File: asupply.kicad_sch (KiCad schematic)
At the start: 94 parts, among them U10 LT3081xDF, U11 LT3042xMSE, U12 LT3045xMSE, U13 LT3045xMSE, U14 LT3042xMSE, U15 LT3094xMSE, U16 LT3042xMSE, U9 LTC3261

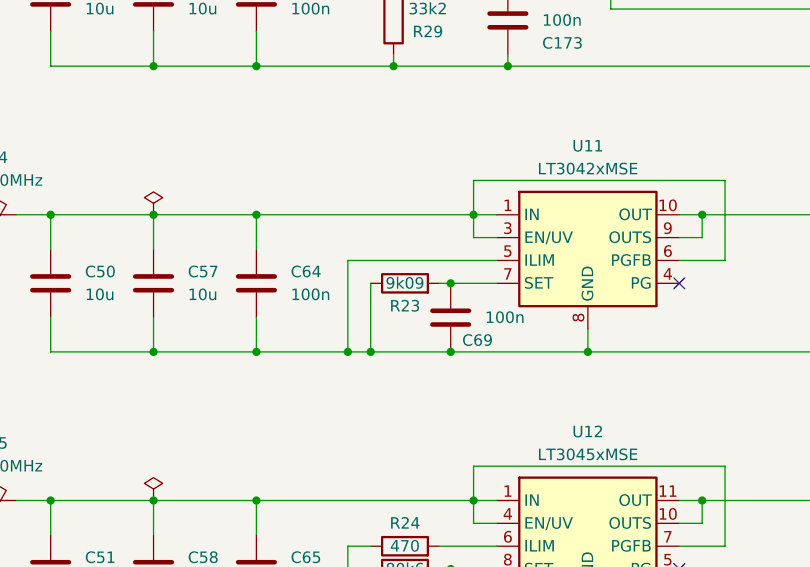
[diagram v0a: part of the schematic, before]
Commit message: add V01 production files, bug fixes
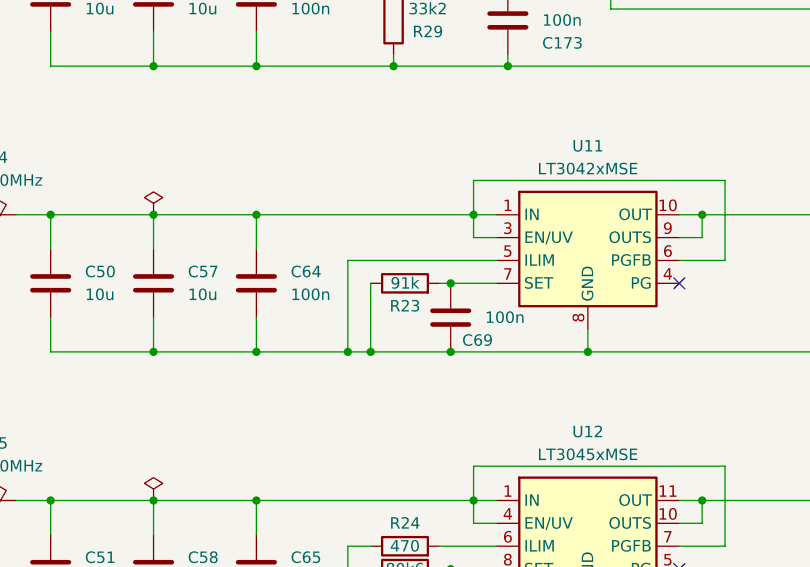
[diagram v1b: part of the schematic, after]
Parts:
- R23: value 9k09 -> 91k
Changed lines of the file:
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@@
     (in_bom yes) (on_board yes)
     (property "Reference" "R23" (id 0) (at 203.2 86.36 90))
-    (property "Value" "9k09" (id 1) (at 203.2 83.82 90))
+    (property "Value" "91k" (id 1) (at 203.2 83.82 90))
     (property "Footprint" "Resistor_SMD:R_0603_1608Metric" (id 2) (at 203.2 85.598 90)
       (effects (font (size 1.27 1.27) bold) hide)

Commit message: v 0.2 schematics
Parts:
- removed C173: 100n, Capacitor_SMD:C_0603_1608Metric, symbol Device:C
- added R?: 51k, Resistor_SMD:R_0603_1608Metric, symbol Device:R
- added TP11, TP12, TP13, TP14, TP15, TP16, TP17, TP18, TP19: TestPoint, TestPoint:TestPoint_Pad_2.0x2.0mm, symbol Connector:TestPoint
- R23: value 91k -> 9k09
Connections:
- net +15V: now also TP19.1
- net +3.3VA: now also TP17.1
- net +5VA: now also TP16.1
- net +8V: now also TP15.1
- net +9V: now also TP13.1
- net +9VA: now also TP14.1
- net -6V: now also TP18.1
- net -9V: now also TP12.1
- net GND: now also R?.1
- net +1V8: now reaches C35.1, C39.1, D5.1 (K), FB8.1
- net +1V8: now also TP11.1
- net LD_EN: now reaches U12.5 (PG)
- net LD_EN: now also R?.2
- no-connect marks 8 -> 7
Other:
- moved on the sheet: C75, C82, C89, U10

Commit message: fixes
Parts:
- added C?: 100n, Capacitor_SMD:C_0603_1608Metric, symbol Device:C
- added C?: 220u, Capacitor_Tantalum_SMD:CP_EIA-7343-15_Kemet-W, symbol Device:C_Polarized
- added C?: 10u, Capacitor_SMD:C_0805_2012Metric, symbol Device:C
- added L?: 1u, Inductor_SMD:L_1008_2520Metric, symbol Device:L
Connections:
- net +9V: now also L?.1; no longer FB2.2
- net GND: now also C?.2, C?.2, C?.2
- new net: C?.1, C?.1, C?.1, FB2.2, L?.2
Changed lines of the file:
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@@
   (junction (at 254 237.49) (diameter 0) (color 0 0 0 0)
   )
+  (junction (at 111.76 168.91) (diameter 0) (color 0 0 0 0)
+  )
   (junction (at 163.83 76.2) (diameter 0) (color 0 0 0 0)
   )
@@
   (junction (at 175.26 107.95) (diameter 0) (color 0 0 0 0)
   )
+  (junction (at 85.09 168.91) (diameter 0) (color 0 0 0 0)
+  )
   (junction (at 196.85 91.44) (diameter 0) (color 0 0 0 0)
   )
@@
   (junction (at 254 219.71) (diameter 0) (color 0 0 0 0)
   )
+  (junction (at 97.79 168.91) (diameter 0) (color 0 0 0 0)
+  )
   (junction (at 148.59 201.93) (diameter 0) (color 0 0 0 0)
   )
@@
   (junction (at 254 201.93) (diameter 0) (color 0 0 0 0)
   )
+  (junction (at 85.09 176.53) (diameter 0) (color 0 0 0 0)
+  )
   (junction (at 110.49 201.93) (diameter 0) (color 0 0 0 0)
   )
@@
   (junction (at 281.94 59.69) (diameter 0) (color 0 0 0 0)
   )
+  (junction (at 97.79 176.53) (diameter 0) (color 0 0 0 0)
+  )
   (junction (at 267.97 59.69) (diameter 0) (color 0 0 0 0)
   )
@@
     (stroke (width 0) (type default) (color 0 0 0 0))
   )
+  (wire (pts (xy 85.09 176.53) (xy 97.79 176.53))
+    (stroke (width 0) (type default) (color 0 0 0 0))
+  )
   (wire (pts (xy 207.01 115.57) (xy 208.28 115.57))
     (stroke (width 0) (type default) (color 0 0 0 0))
@@
     (stroke (width 0) (type default) (color 0 0 0 0))
   )
+  (wire (pts (xy 85.09 168.91) (xy 97.79 168.91))
+    (stroke (width 0) (type default) (color 0 0 0 0))
+  )
   (wire (pts (xy 163.83 59.69) (xy 175.26 59.69))
     (stroke (width 0) (type default) (color 0 0 0 0))
@@
     (stroke (width 0) (type default) (color 0 0 0 0))
   )
+  (wire (pts (xy 115.57 168.91) (xy 111.76 168.91))
+    (stroke (width 0) (type default) (color 0 0 0 0))
+  )
+  (wire (pts (xy 123.19 168.91) (xy 125.73 168.91))
+    (stroke (width 0) (type default) (color 0 0 0 0))
+  )
   (wire (pts (xy 267.97 44.45) (xy 281.94 44.45))
     (stroke (width 0) (type default) (color 0 0 0 0))
@@
     (stroke (width 0) (type default) (color 0 0 0 0))
   )
-  (wire (pts (xy 73.66 189.23) (xy 73.66 193.04))
+  (wire (pts (xy 73.66 168.91) (xy 73.66 193.04))
     (stroke (width 0) (type default) (color 0 0 0 0))
   )
@@
     (stroke (width 0) (type default) (color 0 0 0 0))
   )
+  (wire (pts (xy 73.66 168.91) (xy 85.09 168.91))
+    (stroke (width 0) (type default) (color 0 0 0 0))
+  )
   (wire (pts (xy 267.97 237.49) (xy 267.97 241.3))
     (stroke (width 0) (type default) (color 0 0 0 0))
@@
     (stroke (width 0) (type default) (color 0 0 0 0))
   )
+  (wire (pts (xy 111.76 168.91) (xy 97.79 168.91))
+    (stroke (width 0) (type default) (color 0 0 0 0))
+  )
   (wire (pts (xy 186.69 111.76) (xy 186.69 107.95))
     (stroke (width 0) (type default) (color 0 0 0 0))
@@
     (stroke (width 0) (type default) (color 0 0 0 0))
   )
+  (wire (pts (xy 111.76 176.53) (xy 97.79 176.53))
+    (stroke (width 0) (type default) (color 0 0 0 0))
+  )
   (wire (pts (xy 186.69 184.15) (xy 196.85 184.15))
     (stroke (width 0) (type default) (color 0 0 0 0))
@@
     (pin "2")
   )
+  (symbol (lib_id "Device:C") (at 85.09 172.72 0) (mirror y) (unit 1)
+    (in_bom yes) (on_board yes) (fields_autoplaced)
+    (property "Reference" "C?" (id 0) (at 81.28 171.4499 0)
+      (effects (font (size 1.27 1.27)) (justify left))
+    )
+    (property "Value" "100n" (id 1) (at 81.28 173.9899 0)
+      (effects (font (size 1.27 1.27)) (justify left))
+    )
+    (property "Footprint" "Capacitor_SMD:C_0603_1608Metric" (id 2) (at 84.1248 176.53 0)
+      (effects (font (size 1.27 1.27)) hide)
+    )
+    (property "Datasheet" "~" (id 3) (at 85.09 172.72 0)
+      (effects (font (size 1.27 1.27)) hide)
+    )
+    (property "MFR_PN" "CL10B104KB8NNWC" (id 4) (at 85.09 172.72 0)
+      (effects (font (size 1.27 1.27)) hide)
+    )
+    (property "MFR_PN_ALT" "CL10B104KB8NNNL" (id 5) (at 85.09 172.72 0)
+      (effects (font (size 1.27 1.27)) hide)
+    )
+    (pin "1")
+    (pin "2")
+  )
   (symbol (lib_id "Device:C") (at 254 83.82 0) (unit 1)
     (in_bom yes) (on_board yes) (fields_autoplaced)
@@
     (pin "2")
   )
+  (symbol (lib_id "Device:C_Polarized") (at 111.76 172.72 0) (mirror y) (unit 1)
+    (in_bom yes) (on_board yes) (fields_autoplaced)
+    (property "Reference" "C?" (id 0) (at 107.95 170.5609 0)
+      (effects (font (size 1.27 1.27)) (justify left))
+    )
+    (property "Value" "220u" (id 1) (at 107.95 173.1009 0)
+      (effects (font (size 1.27 1.27)) (justify left))
+    )
+    (property "Footprint" "Capacitor_Tantalum_SMD:CP_EIA-7343-15_Kemet-W" (id 2) (at 110.7948 176.53 0)
+      (effects (font (size 1.27 1.27)) hide)
+    )
+    (property "Datasheet" "~" (id 3) (at 111.76 172.72 0)
+      (effects (font (size 1.27 1.27)) hide)
+    )
+    (property "MFR_PN" "T491D227K016AT" (id 4) (at 111.76 172.72 0)
+      (effects (font (size 1.27 1.27)) hide)
+    )
+    (property "MFR_PN_ALT" "293D227X9016E2TE3" (id 5) (at 111.76 172.72 0)
+      (effects (font (size 1.27 1.27)) hide)
+    )
+    (pin "1")
+    (pin "2")
+  )
   (symbol (lib_id "Device:C") (at 254 245.11 0) (unit 1)
     (in_bom yes) (on_board yes) (fields_autoplaced)
@@
     (pin "2")
   )
+  (symbol (lib_id "Device:C") (at 97.79 172.72 0) (mirror y) (unit 1)
+    (in_bom yes) (on_board yes) (fields_autoplaced)
+    (property "Reference" "C?" (id 0) (at 93.98 171.4499 0)
+      (effects (font (size 1.27 1.27)) (justify left))
+    )
+    (property "Value" "10u" (id 1) (at 93.98 173.9899 0)
+      (effects (font (size 1.27 1.27)) (justify left))
+    )
+    (property "Footprint" "Capacitor_SMD:C_0805_2012Metric" (id 2) (at 96.8248 176.53 0)
+      (effects (font (size 1.27 1.27)) hide)
+    )
+    (property "Datasheet" "~" (id 3) (at 97.79 172.72 0)
+      (effects (font (size 1.27 1.27)) hide)
+    )
+    (property "MFR_PN" "CL21B106KOQNNNG" (id 4) (at 97.79 172.72 0)
+      (effects (font (size 1.27 1.27)) hide)
+    )
+    (property "MFR_PN_ALT" "CL21B106KOQNNNE" (id 5) (at 97.79 172.72 0)
+      (effects (font (size 1.27 1.27)) hide)
+    )
+    (pin "1")
+    (pin "2")
+  )
   (symbol (lib_id "Device:C") (at 281.94 83.82 0) (unit 1)
     (in_bom yes) (on_board yes) (fields_autoplaced)
@@
     (pin "2")
   )
+  (symbol (lib_id "Device:L") (at 119.38 168.91 270) (mirror x) (unit 1)
+    (in_bom yes) (on_board yes) (fields_autoplaced)
+    (property "Reference" "L?" (id 0) (at 119.38 162.56 90))
+    (property "Value" "1u" (id 1) (at 119.38 165.1 90))
+    (property "Footprint" "Inductor_SMD:L_1008_2520Metric" (id 2) (at 119.38 168.91 0)
+      (effects (font (size 1.27 1.27)) hide)
+    )
+    (property "Datasheet" "~" (id 3) (at 119.38 168.91 0)
+      (effects (font (size 1.27 1.27)) hide)
+    )
+    (property "MFR_PN" "DFE252012F-1R0M=P2" (id 4) (at 119.38 168.91 0)
+      (effects (font (size 1.27 1.27)) hide)
+    )
+    (property "MFR_PN_ALT" "DFE252012P-1R0M=P2" (id 5) (at 119.38 168.91 0)
+      (effects (font (size 1.27 1.27)) hide)
+    )
+    (pin "1")
+    (pin "2")
+  )
   (symbol (lib_id "Device:C") (at 254 176.53 0) (unit 1)
     (in_bom yes) (on_board yes) (fields_autoplaced)
@@
     (pin "2")
   )
-  (symbol (lib_id "power:+9V") (at 73.66 189.23 0) (unit 1)
+  (symbol (lib_id "power:+9V") (at 125.73 168.91 270) (unit 1)
     (in_bom yes) (on_board yes) (fields_autoplaced)
-    (property "Reference" "#PWR058" (id 0) (at 73.66 193.04 0)
+    (property "Reference" "#PWR058" (id 0) (at 121.92 168.91 0)
       (effects (font (size 1.27 1.27)) hide)
     )
-    (property "Value" "+9V" (id 1) (at 73.66 184.15 0))
-    (property "Footprint" "" (id 2) (at 73.66 189.23 0)
+    (property "Value" "+9V" (id 1) (at 129.54 168.9099 90)
+      (effects (font (size 1.27 1.27)) (justify left))
+    )
+    (property "Footprint" "" (id 2) (at 125.73 168.91 0)
       (effects (font (size 1.27 1.27)) hide)
     )
-    (property "Datasheet" "" (id 3) (at 73.66 189.23 0)
+    (property "Datasheet" "" (id 3) (at 125.73 168.91 0)
       (effects (font (size 1.27 1.27)) hide)
     )
@@
     (pin "2")
   )
+  (symbol (lib_id "power:GND") (at 85.09 176.53 0) (mirror y) (unit 1)
+    (in_bom yes) (on_board yes) (fields_autoplaced)
+    (property "Reference" "#PWR?" (id 0) (at 85.09 182.88 0)
+      (effects (font (size 1.27 1.27)) hide)
+    )
+    (property "Value" "GND" (id 1) (at 85.09 181.61 0))
+    (property "Footprint" "" (id 2) (at 85.09 176.53 0)
+      (effects (font (size 1.27 1.27)) hide)
+    )
+    (property "Datasheet" "" (id 3) (at 85.09 176.53 0)
+      (effects (font (size 1.27 1.27)) hide)
+    )
+    (pin "1")
+  )
   (symbol (lib_id "power:GND") (at 101.6 194.31 180) (unit 1)

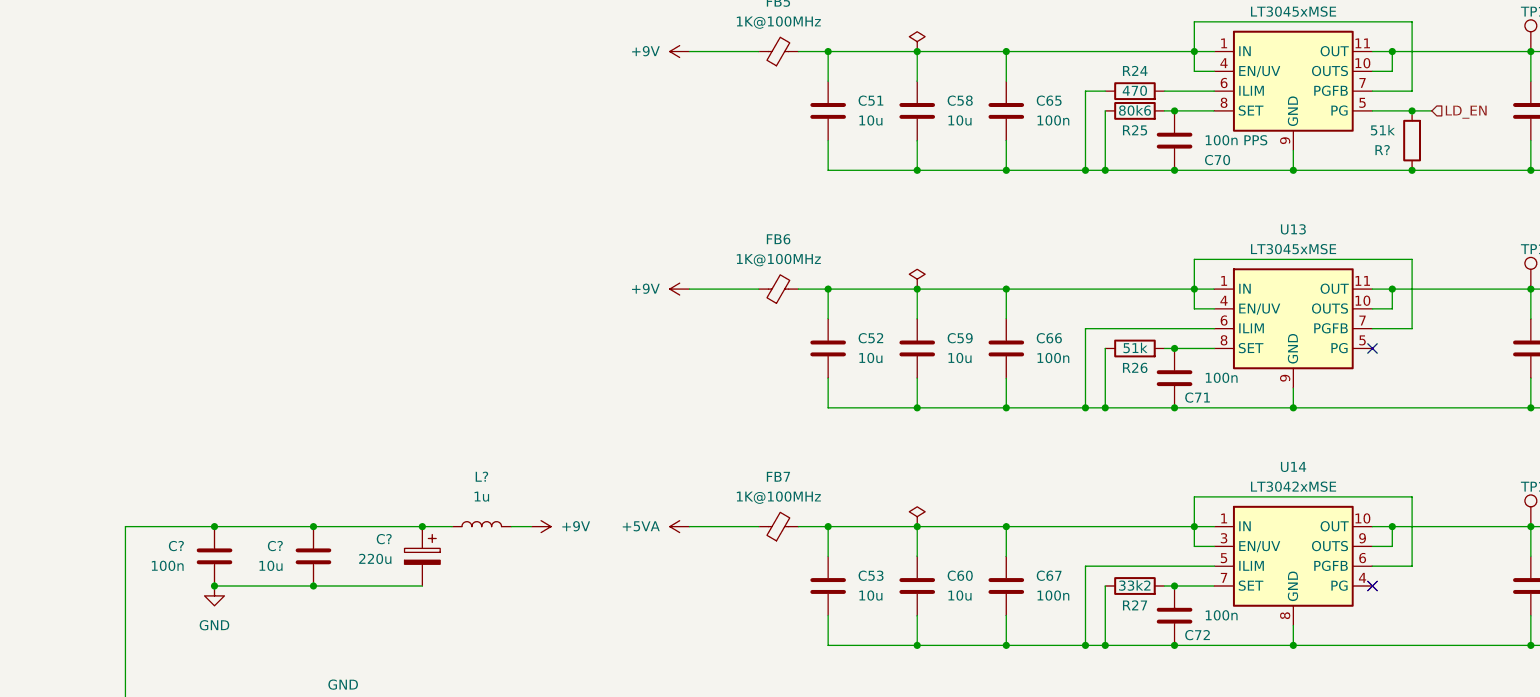
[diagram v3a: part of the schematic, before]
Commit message: change damper
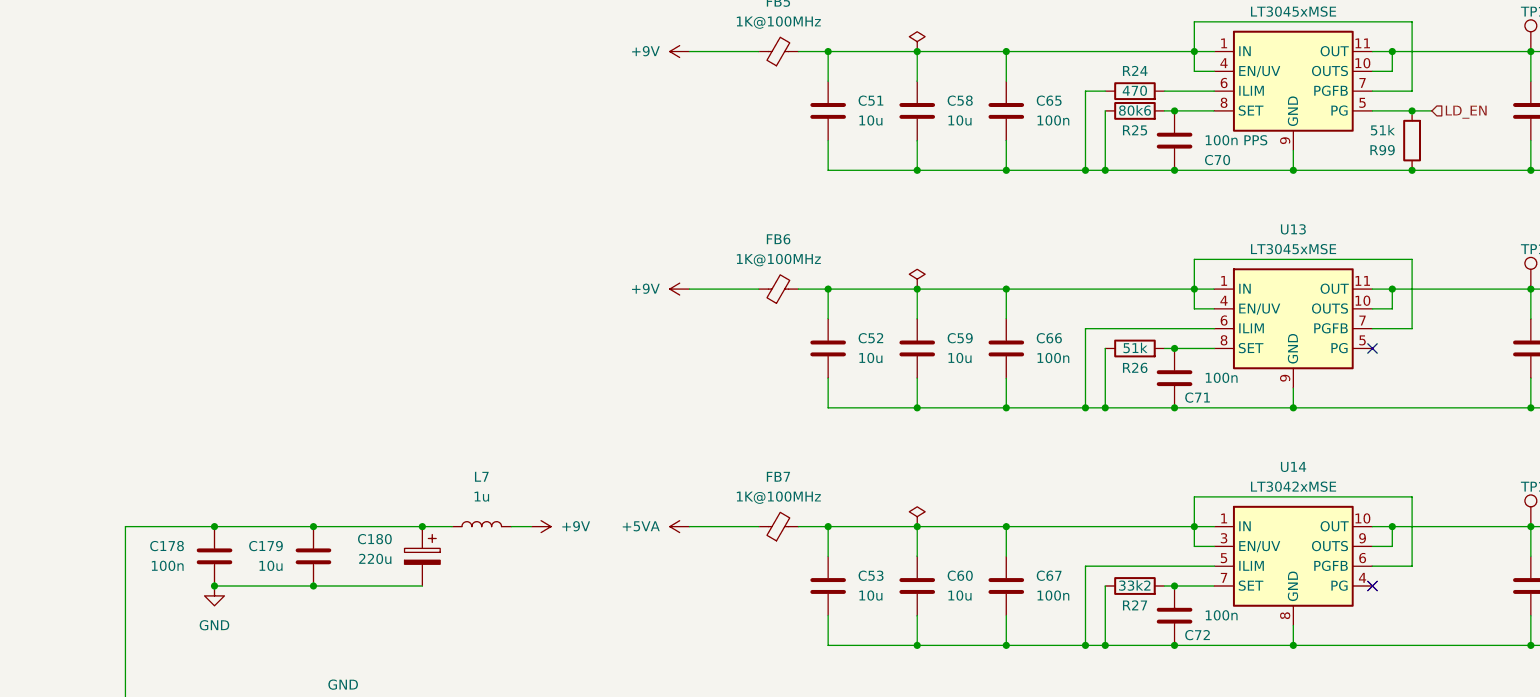
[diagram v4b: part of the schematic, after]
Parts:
- gave numbers to parts that had none: 5
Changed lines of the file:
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@@
   (symbol (lib_id "Device:C") (at 85.09 172.72 0) (mirror y) (unit 1)
     (in_bom yes) (on_board yes) (fields_autoplaced)
-    (property "Reference" "C?" (id 0) (at 81.28 171.4499 0)
+    (property "Reference" "C178" (id 0) (at 81.28 171.4499 0)
       (effects (font (size 1.27 1.27)) (justify left))
     )
@@
   (symbol (lib_id "Device:R") (at 238.76 119.38 180) (unit 1)
     (in_bom yes) (on_board yes)
-    (property "Reference" "R?" (id 0) (at 234.95 120.65 0))
+    (property "Reference" "R99" (id 0) (at 234.95 120.65 0))
     (property "Value" "51k" (id 1) (at 234.95 118.11 0))
     (property "Footprint" "Resistor_SMD:R_0603_1608Metric" (id 2) (at 240.538 119.38 90)
@@
   (symbol (lib_id "Device:C_Polarized") (at 111.76 172.72 0) (mirror y) (unit 1)
     (in_bom yes) (on_board yes) (fields_autoplaced)
-    (property "Reference" "C?" (id 0) (at 107.95 170.5609 0)
+    (property "Reference" "C180" (id 0) (at 107.95 170.5609 0)
       (effects (font (size 1.27 1.27)) (justify left))
     )
@@
   (symbol (lib_id "Device:C") (at 97.79 172.72 0) (mirror y) (unit 1)
     (in_bom yes) (on_board yes) (fields_autoplaced)
-    (property "Reference" "C?" (id 0) (at 93.98 171.4499 0)
+    (property "Reference" "C179" (id 0) (at 93.98 171.4499 0)
       (effects (font (size 1.27 1.27)) (justify left))
     )
@@
   (symbol (lib_id "Device:L") (at 119.38 168.91 270) (mirror x) (unit 1)
     (in_bom yes) (on_board yes) (fields_autoplaced)
-    (property "Reference" "L?" (id 0) (at 119.38 162.56 90))
+    (property "Reference" "L7" (id 0) (at 119.38 162.56 90))
     (property "Value" "1u" (id 1) (at 119.38 165.1 90))
     (property "Footprint" "Inductor_SMD:L_1008_2520Metric" (id 2) (at 119.38 168.91 0)
@@
   (symbol (lib_id "power:GND") (at 85.09 176.53 0) (mirror y) (unit 1)
     (in_bom yes) (on_board yes) (fields_autoplaced)
-    (property "Reference" "#PWR?" (id 0) (at 85.09 182.88 0)
-      (effects (font (size 1.27 1.27)) hide)
-    )
+    (property "Reference" "#PWR0164" (id 0) (at 85.09 182.88 0)
+      (effects (font (size 1.27 1.27)) hide)
+    )

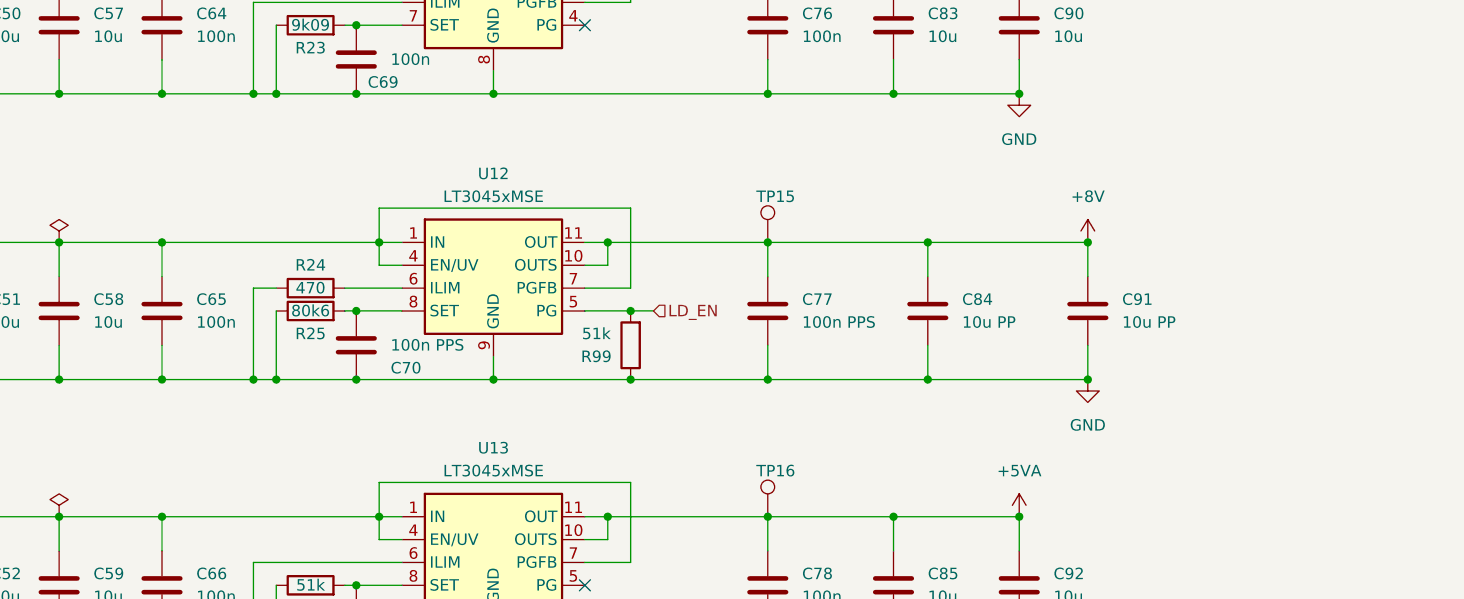
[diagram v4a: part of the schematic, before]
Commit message: change PD LD circuit
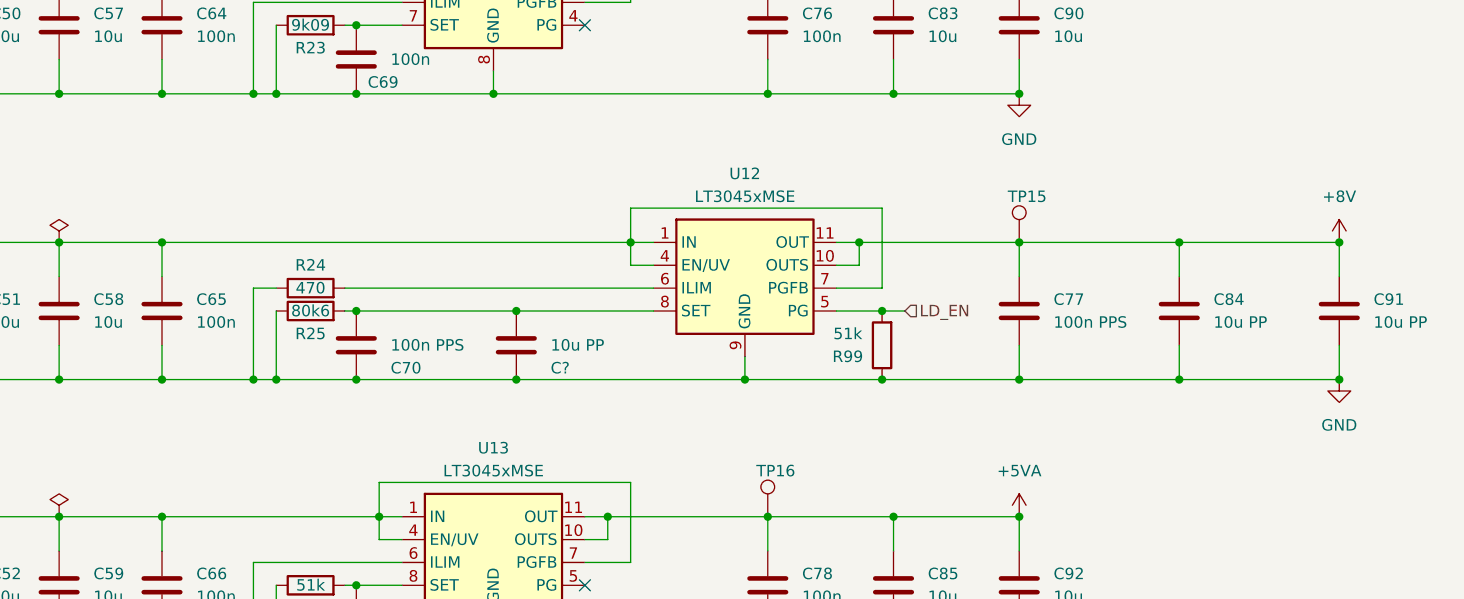
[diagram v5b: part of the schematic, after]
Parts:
- added C?: 10u PP, Capacitor_SMD:C_1812_4532Metric, symbol Device:C
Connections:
- net GND: now also C?.2
- net at C70.1, R25.2, U12.8 (SET): now also C?.1
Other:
- moved on the sheet: C77, C84, C91, R99, TP15, U12
